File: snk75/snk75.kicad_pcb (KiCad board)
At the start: 2 copper layers, 314.3 x 123.8 mm, 339 parts, among them J1 TYPE-C-31-M12, Q1 AO3400A, U1 STM32F072C8Tx, U2 XC6206P332MR, U3 USBLC6-2SC6, U4 SGM2007-3.3XN5/TR

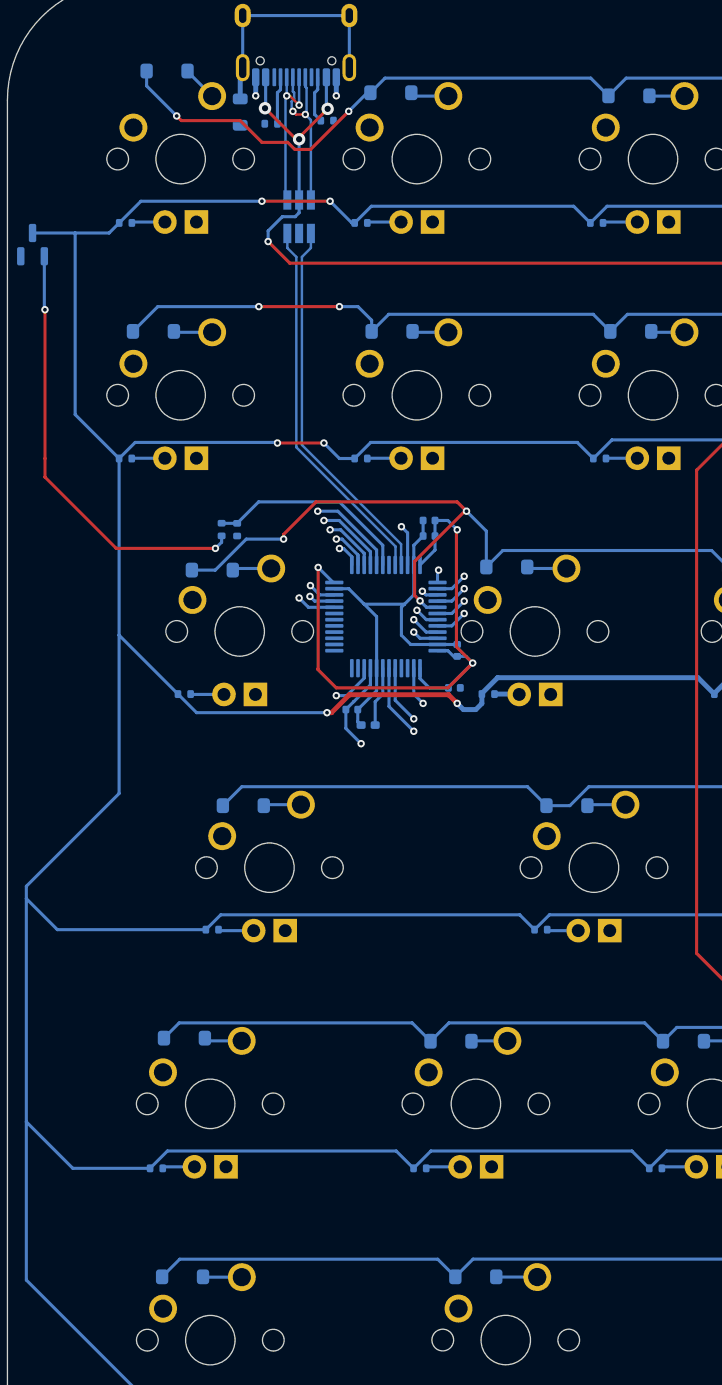
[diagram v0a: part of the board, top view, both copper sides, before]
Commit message: Routed rows to MCU and began cols
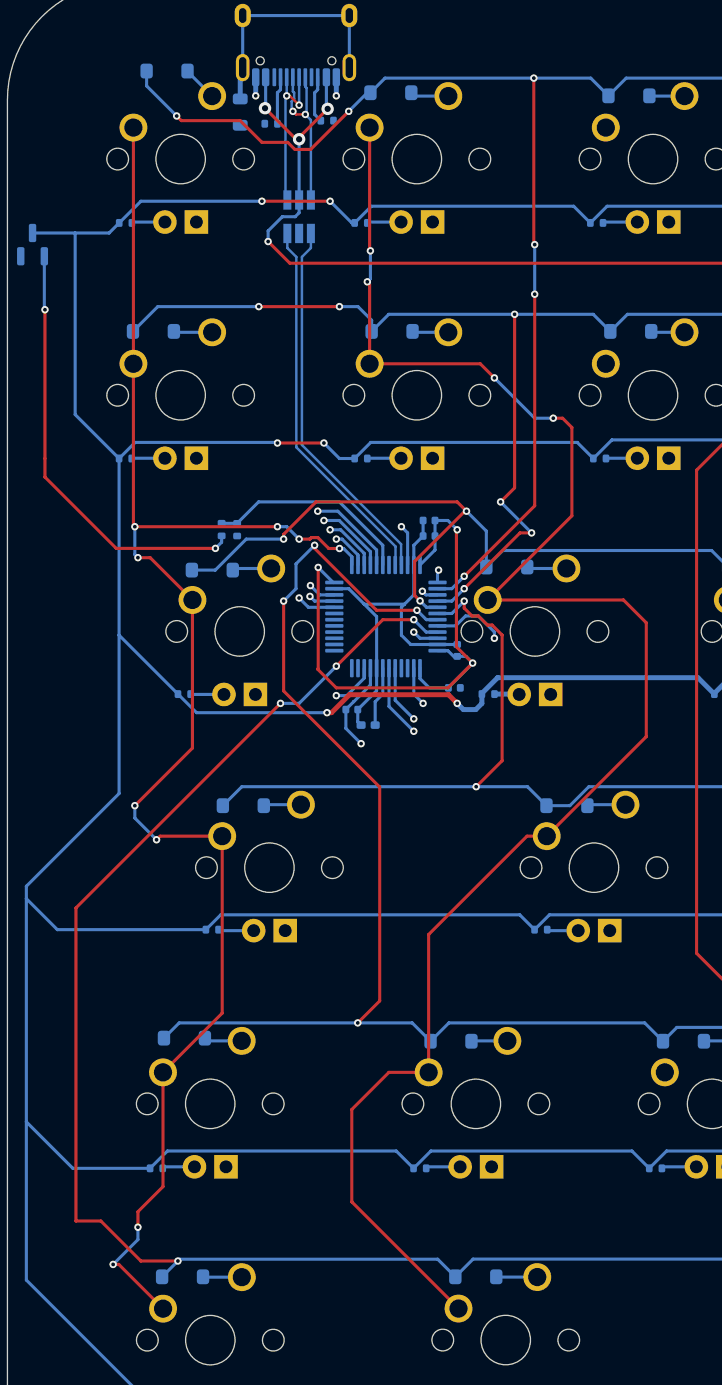
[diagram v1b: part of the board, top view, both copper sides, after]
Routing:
- net col2: track 3.08 -> 142.6 mm, vias 1 -> 5
- net col1: track 1.95 -> 131.0 mm, vias 1 -> 9
- net row6: track 300.2 -> 371.9 mm, vias 3 -> 6
- net row5: track 302.3 -> 356.4 mm, vias 1 -> 4
- net row1: track 309.3 -> 351.8 mm, vias 3 -> 6
- net row2: track 309.3 -> 335.7 mm, vias 3 -> 6
- net row4: track 299.3 -> 316.9 mm, vias 3 -> 4
- net BOOT: track 2.57 -> 5.96 mm

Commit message: WIP: Removed wrong path, gonna rebuild with better designed path
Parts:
- C19, C20: footprint Capacitor_Tantalum_SMD:CP_EIA-3528-21_Kemet-B -> Capacitor_SMD:C_0402_1005Metric
- C21: footprint Capacitor_Tantalum_SMD:CP_EIA-3216-18_Kemet-A -> Capacitor_SMD:C_0402_1005Metric
- moved C21 194.3 mm to (14.2, 81.0)
- moved C20 177.6 mm to (14.2, 82.0)
- moved C23 176.8 mm to (14.3, 78.0)
- moved C19 175.0 mm to (14.2, 80.0)
- moved C22 171.8 mm to (14.3, 79.0)
- moved C25 171.6 mm to (19.8, 82.0), turned to 0 degrees
- moved R110 131.7 mm to (-6.15, 65.8), turned to 90 degrees
- moved D102 131.4 mm to (-7.90, 62.0), turned to 90 degrees
- moved C34 131.2 mm to (-7.65, 66.2), turned to 90 degrees
- moved U4 125.6 mm to (-5.70, 62.1), turned to -90 degrees
- moved R109 123.7 mm to (-5.41, 58.8), turned to 180 degrees
- moved C33 122.6 mm to (-3.65, 62.7), turned to -90 degrees
- moved C31 122.6 mm to (-5.35, 57.0), turned to 180 degrees
- moved F1 121.3 mm to (-5.20, 54.7), turned to 180 degrees
- moved C32 84.3 mm to (14.8, 72.3), turned to -90 degrees
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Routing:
- net VBUS: track 174.4 -> 45.0 mm, vias 5 -> 4
- net col10: track 0.00 -> 112.2 mm
- net col11: track 4.71 -> 113.2 mm, vias 1 -> 0
- net col15: track 2.12 -> 110.0 mm, vias 1 -> 0
- net col12: track 5.92 -> 112.2 mm, vias 1 -> 0
- net col3: track 4.47 -> 109.0 mm, vias 1 -> 0
- net col7: track 3.29 -> 106.2 mm, vias 1 -> 0
- net col13: track 3.64 -> 105.1 mm, vias 1 -> 0
- net col14: track 3.15 -> 103.6 mm, vias 1 -> 0
- net col8: track 1.04 -> 87.1 mm, vias 1 -> 0
- net col9: track 2.12 -> 86.8 mm, vias 1 -> 0
- net col6: track 3.15 -> 86.9 mm, vias 1 -> 0
- net col4: track 5.87 -> 87.1 mm, vias 1 -> 0
- net col5: track 7.26 -> 87.0 mm, vias 1 -> 0
- net row6: track 371.9 -> 297.9 mm, vias 6 -> 0
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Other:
- outline, holes or cut-outs redrawn
